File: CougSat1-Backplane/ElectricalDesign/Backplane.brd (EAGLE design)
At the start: 82.8 x 86 mm, 17 parts, among them J1 CougSat Socket, J10 CougSat Socket, J2 CougSat Socket, J3 CougSat Socket, J4 CougSat Socket, J5 Separation Switch, J6 Separation Switch, J7 CougSat Socket, J8 CougSat Socket, J9 CougSat Socket

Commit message: Added balancing and silkscreen decals
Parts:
- added LOGO100: Satellite 16mm, CougsInSpace-Aesthetics:CIS-SATELLITE-16
- added LOGO2: SIGNATUREHENDRIK, CougsInSpace-Aesthetics:SIGN-HENDRIK
- LOGO1: value SIGNATUREHENDRIK -> Text; device CougsInSpace-Aesthetics:SIGN-HENDRIK -> CougsInSpace-Aesthetics:CIS-TEXT
- moved LOGO1 40.6 mm to (-25.3, 0.00)
- moved H1 28.0 mm to (-14.0, 0.00)
- moved H2 28.0 mm to (14.0, 0.00)
- moved C1 19.3 mm to (-9.50, -1.80), turned to 270 degrees
- moved C2 19.0 mm to (9.50, -1.80)
- moved R2 3.60 mm to (9.50, 1.80), turned to 270 degrees
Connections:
- net CHASSIS1: now also C1.1, H1.1, H1.V1, H1.V2, H1.V3, H1.V4, H1.V5, H1.V6, H1.V7, H1.V8; no longer C2.1, H2.1, H2.V1, H2.V2, H2.V3, H2.V4, H2.V5, H2.V6, H2.V7, H2.V8
- net CHASSIS2: now also C2.1, H2.1, H2.V1, H2.V2, H2.V3, H2.V4, H2.V5, H2.V6, H2.V7, H2.V8; no longer C1.1, H1.1, H1.V1, H1.V2, H1.V3, H1.V4, H1.V5, H1.V6, H1.V7, H1.V8
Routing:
- net PGND: track 395.8 -> 389.8 mm
- net CHASSIS2: track 25.9 -> 26.5 mm
- added copper zone on layer 1, net BALANCING-TOP
- added copper zone on layer 16, net BALANCING-TOP
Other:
- board text added: "Backplane V3.0 1915"

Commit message: Final asthetic changes, re-exported pdfs
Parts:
- moved LOGO100 25.8 mm to (-29.2, 25.7), flipped to the top
- moved J5 3.00 mm to (-29.0, 0.00)
- moved J6 3.00 mm to (29.0, 0.00)
- moved LOGO2 0.50 mm to (25.5, 0.00)
- moved LOGO1 0.10 mm to (-25.2, 0.00), flipped to the bottom
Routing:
- net PWR_CTRL_SW: track 218.1 -> 214.4 mm
- net PGND: track 389.8 -> 386.1 mm
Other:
- board text added: "Backplane V3.0"
- board text added: "Slot 0"
- board text added: "Slot 1"
- board text added: "Slot 2"
- board text added: "Slot 3"
- board text added: "Slot 4"
- board text added: "Slot 5"
- board text added: "Slot 6"
- board text added: "Slot 7"
- board text removed: "Backplane V3.0 1915"

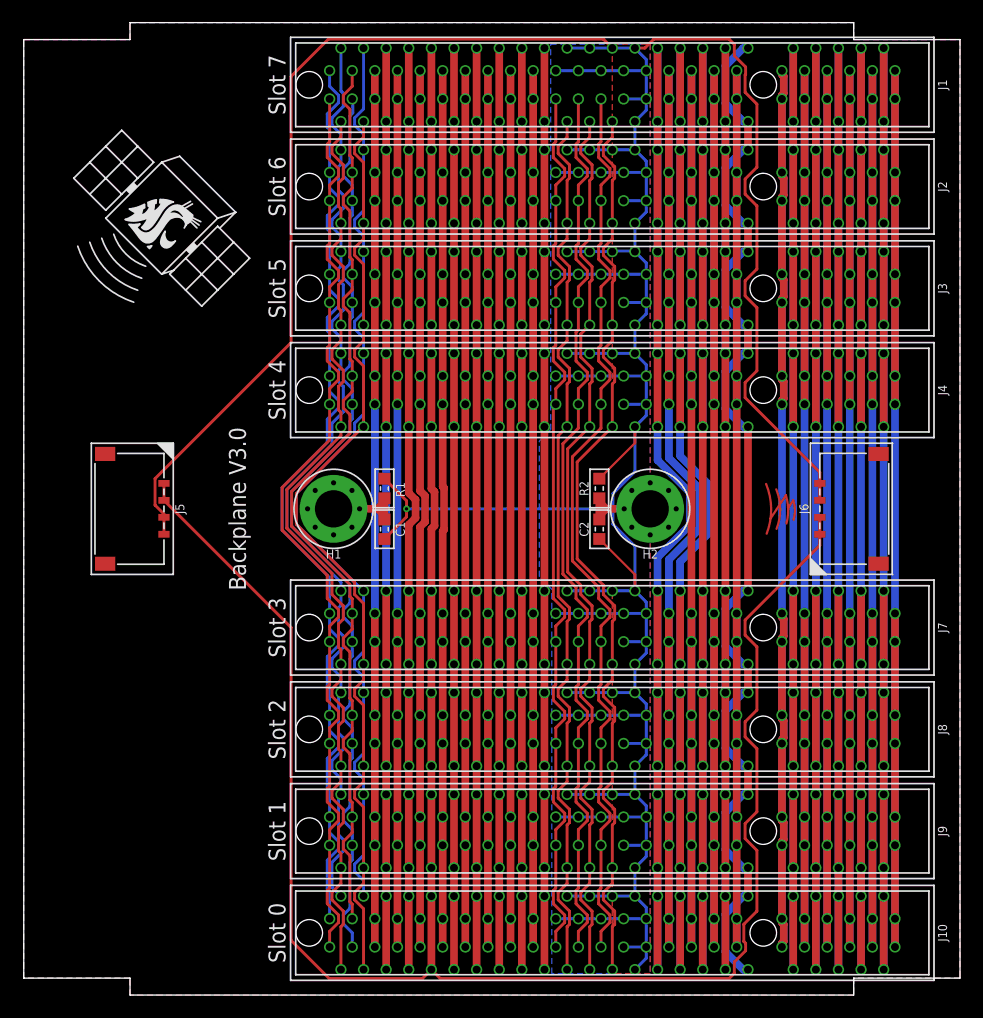
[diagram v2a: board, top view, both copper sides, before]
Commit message: Fixed dimension errors, updated signature
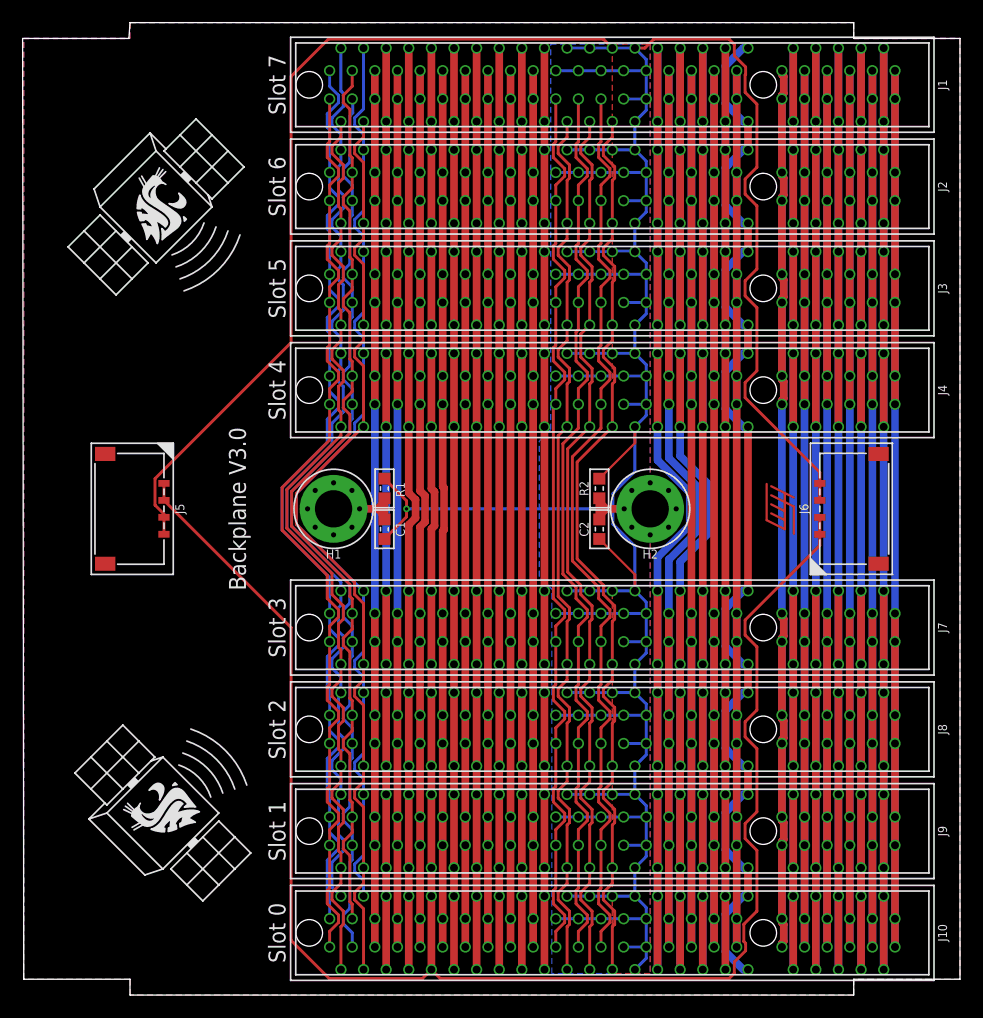
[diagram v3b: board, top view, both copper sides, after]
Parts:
- added LOGO3: Satellite 16mm, CougsInSpace-Aesthetics:CIS-SATELLITE-16
- moved LOGO1 3.20 mm to (-28.4, 0.10)
- moved LOGO100 1.12 mm to (-29.7, 26.7), turned to 90 degrees
- turned LOGO2 to 270 degrees
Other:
- board size 82.8 x 86 mm -> 82.9 x 86 mm
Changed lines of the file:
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@@
 <setting verticaltext="up"/>
 </settings>
-<grid distance="0.25" unitdist="mm" unit="mm" style="lines" multiple="1" display="yes" altdistance="0.05" altunitdist="mm" altunit="mm"/>
+<grid distance="0.1" unitdist="mm" unit="mm" style="lines" multiple="1" display="yes" altdistance="0.005" altunitdist="mm" altunit="mm"/>
 <layers>
 <layer number="1" name="Top" color="4" fill="1" visible="yes" active="yes"/>
@@
 <board>
 <plain>
-<wire x1="41.4" y1="-41.5" x2="32" y2="-41.5" width="0" layer="20"/>
-<wire x1="32" y1="-41.5" x2="32" y2="-43" width="0" layer="20"/>
+<wire x1="41.4" y1="-41.6" x2="32" y2="-41.6" width="0" layer="20"/>
+<wire x1="32" y1="-41.6" x2="32" y2="-43" width="0" layer="20"/>
 <wire x1="32" y1="-43" x2="-32" y2="-43" width="0" layer="20"/>
-<wire x1="-32" y1="-43" x2="-32" y2="-41.5" width="0" layer="20"/>
-<wire x1="-32" y1="-41.5" x2="-41.4" y2="-41.5" width="0" layer="20"/>
-<wire x1="-41.4" y1="-41.5" x2="-41.4" y2="41.5" width="0" layer="20"/>
-<wire x1="-41.4" y1="41.5" x2="-32" y2="41.5" width="0" layer="20"/>
-<wire x1="-32" y1="41.5" x2="-32" y2="43" width="0" layer="20"/>
+<wire x1="-32" y1="-43" x2="-32" y2="-41.6" width="0" layer="20"/>
+<wire x1="-32" y1="-41.6" x2="-41.4" y2="-41.6" width="0" layer="20"/>
+<wire x1="-41.4" y1="-41.6" x2="-41.5" y2="41.6" width="0" layer="20"/>
+<wire x1="-41.5" y1="41.6" x2="-32.1" y2="41.6" width="0" layer="20"/>
+<wire x1="-32.1" y1="41.6" x2="-32" y2="43" width="0" layer="20"/>
 <wire x1="-32" y1="43" x2="32" y2="43" width="0" layer="20"/>
-<wire x1="32" y1="43" x2="32" y2="41.5" width="0" layer="20"/>
-<wire x1="32" y1="41.5" x2="41.4" y2="41.5" width="0" layer="20"/>
-<wire x1="41.4" y1="41.5" x2="41.4" y2="-41.5" width="0" layer="20"/>
+<wire x1="32" y1="43" x2="32" y2="41.6" width="0" layer="20"/>
+<wire x1="32" y1="41.6" x2="41.4" y2="41.6" width="0" layer="20"/>
+<wire x1="41.4" y1="41.6" x2="41.4" y2="-41.6" width="0" layer="20"/>
 <text x="-22.5" y="0" size="1.5" layer="21" font="vector" ratio="15" rot="R90" align="center">Backplane V3.0</text>
 <text x="-19" y="-37.5" size="1.5" layer="21" font="vector" ratio="15" rot="R270" align="center">Slot 0</text>
@@
 <attribute name="TEMP" value="70°C Max 2A" x="-85.75" y="-37.57" size="1.778" layer="27" rot="R270" display="off"/>
 </element>
-<element name="LOGO2" library="CougsInSpace-Aesthetics" package="SIGN-HENDRIK" value="SIGNATUREHENDRIK" x="25.5" y="0" smashed="yes"/>
-<element name="LOGO1" library="CougsInSpace-Aesthetics" package="CIS-TEXT" value="Text" x="-25.2" y="0" smashed="yes" rot="MR90"/>
-<element name="LOGO100" library="CougsInSpace-Aesthetics" package="CIS-SATELLITE-16" value="Satellite 16mm" x="-29.2" y="25.7" smashed="yes"/>
+<element name="LOGO2" library="CougsInSpace-Aesthetics" package="SIGN-HENDRIK" value="SIGNATUREHENDRIK" x="25.5" y="0" smashed="yes" rot="R270"/>
+<element name="LOGO1" library="CougsInSpace-Aesthetics" package="CIS-TEXT" value="Text" x="-28.4" y="0.1" smashed="yes" rot="MR90"/>
+<element name="LOGO100" library="CougsInSpace-Aesthetics" package="CIS-SATELLITE-16" value="Satellite 16mm" x="-29.7" y="26.7" smashed="yes" rot="R90"/>
+<element name="LOGO3" library="CougsInSpace-Aesthetics" package="CIS-SATELLITE-16" value="Satellite 16mm" x="-29.1" y="-26.9" smashed="yes" rot="R180"/>
 </elements>
 <signals>
@@
 <signal name="BALANCING-TOP">
 <polygon width="0.16" layer="1" spacing="0.5" pour="hatch" rank="6">
-<vertex x="-41.4" y="41.5"/>
-<vertex x="-32" y="41.5"/>
+<vertex x="-41.4" y="41.6"/>
+<vertex x="-32" y="41.6"/>
 <vertex x="-32" y="43"/>
 <vertex x="32" y="43"/>
-<vertex x="32" y="41.5"/>
-<vertex x="41.4" y="41.5"/>
-<vertex x="41.4" y="-41.5"/>
-<vertex x="32" y="-41.5"/>
+<vertex x="32" y="41.6"/>
+<vertex x="41.4" y="41.6"/>
+<vertex x="41.4" y="-41.6"/>
+<vertex x="32" y="-41.6"/>
 <vertex x="32" y="-43"/>
 <vertex x="-32" y="-43"/>
-<vertex x="-32" y="-41.5"/>
-<vertex x="-41.4" y="-41.5"/>
+<vertex x="-32" y="-41.6"/>
+<vertex x="-41.4" y="-41.6"/>
 </polygon>
 <polygon width="0.16" layer="16" spacing="0.5" pour="hatch" rank="6">
-<vertex x="-41.4" y="41.5"/>
-<vertex x="-32" y="41.5"/>
+<vertex x="-41.4" y="41.6"/>
+<vertex x="-32" y="41.6"/>
 <vertex x="-32" y="43"/>
 <vertex x="32" y="43"/>
-<vertex x="32" y="41.5"/>
-<vertex x="41.4" y="41.5"/>
-<vertex x="41.4" y="-41.5"/>
-<vertex x="32" y="-41.5"/>
+<vertex x="32" y="41.6"/>
+<vertex x="41.4" y="41.6"/>
+<vertex x="41.4" y="-41.6"/>
+<vertex x="32" y="-41.6"/>
 <vertex x="32" y="-43"/>
 <vertex x="-32" y="-43"/>
-<vertex x="-32" y="-41.5"/>
-<vertex x="-41.4" y="-41.5"/>
+<vertex x="-32" y="-41.6"/>
+<vertex x="-41.4" y="-41.6"/>
 </polygon>
 </signal>
 </signals>
 <mfgpreviewcolors>
-<mfgpreviewcolor name="soldermaskcolor" color="0xC8008000"/>
+<mfgpreviewcolor name="soldermaskcolor" color="0xC8FF0000"/>
 <mfgpreviewcolor name="silkscreencolor" color="0xFFFEFEFE"/>
 <mfgpreviewcolor name="backgroundcolor" color="0xFF282828"/>

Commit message: Fixed Board Outline and Updated mCAD
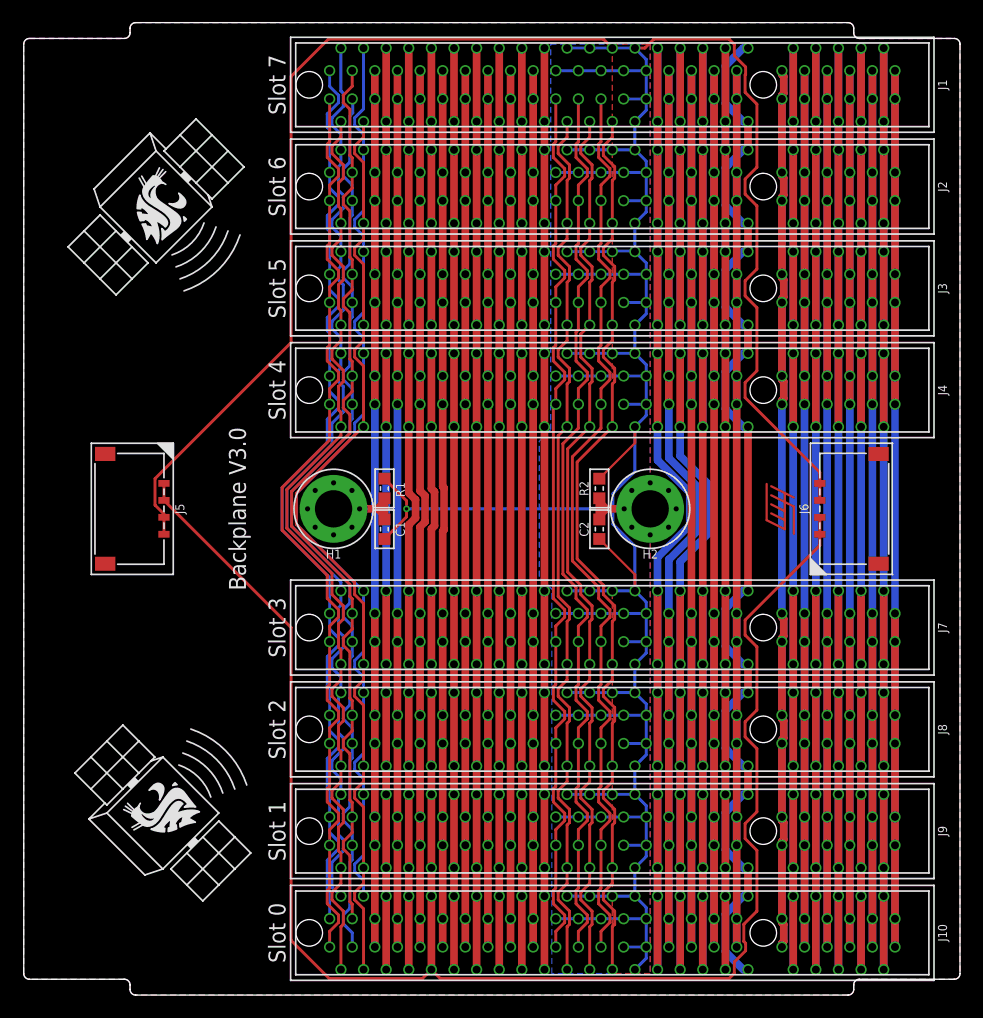
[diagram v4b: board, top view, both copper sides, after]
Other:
- board size 82.9 x 86 mm -> 82.8 x 86 mm
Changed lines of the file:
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@@
 <board>
 <plain>
-<wire x1="41.4" y1="-41.6" x2="32" y2="-41.6" width="0" layer="20"/>
-<wire x1="32" y1="-41.6" x2="32" y2="-43" width="0" layer="20"/>
-<wire x1="32" y1="-43" x2="-32" y2="-43" width="0" layer="20"/>
-<wire x1="-32" y1="-43" x2="-32" y2="-41.6" width="0" layer="20"/>
-<wire x1="-32" y1="-41.6" x2="-41.4" y2="-41.6" width="0" layer="20"/>
-<wire x1="-41.4" y1="-41.6" x2="-41.5" y2="41.6" width="0" layer="20"/>
-<wire x1="-41.5" y1="41.6" x2="-32.1" y2="41.6" width="0" layer="20"/>
-<wire x1="-32.1" y1="41.6" x2="-32" y2="43" width="0" layer="20"/>
-<wire x1="-32" y1="43" x2="32" y2="43" width="0" layer="20"/>
-<wire x1="32" y1="43" x2="32" y2="41.6" width="0" layer="20"/>
-<wire x1="32" y1="41.6" x2="41.4" y2="41.6" width="0" layer="20"/>
-<wire x1="41.4" y1="41.6" x2="41.4" y2="-41.6" width="0" layer="20"/>
+<wire x1="-31.5" y1="43" x2="31.5" y2="43" width="0" layer="20"/>
+<wire x1="31.5" y1="43" x2="32" y2="42.5" width="0" layer="20" curve="-90"/>
+<wire x1="32" y1="42.5" x2="32" y2="42.1" width="0" layer="20"/>
+<wire x1="32" y1="42.1" x2="32.5" y2="41.6" width="0" layer="20" curve="90"/>
+<wire x1="32.5" y1="41.6" x2="40.9" y2="41.6" width="0" layer="20"/>
+<wire x1="40.9" y1="41.6" x2="41.4" y2="41.1" width="0" layer="20" curve="-90"/>
+<wire x1="41.4" y1="41.1" x2="41.4" y2="-41.1" width="0" layer="20"/>
+<wire x1="41.4" y1="-41.1" x2="40.9" y2="-41.6" width="0" layer="20" curve="-90"/>
+<wire x1="40.9" y1="-41.6" x2="32.5" y2="-41.6" width="0" layer="20"/>
+<wire x1="32.5" y1="-41.6" x2="32" y2="-42.1" width="0" layer="20" curve="90"/>
+<wire x1="32" y1="-42.1" x2="32" y2="-42.5" width="0" layer="20"/>
+<wire x1="32" y1="-42.5" x2="31.5" y2="-43" width="0" layer="20" curve="-90"/>
+<wire x1="31.5" y1="-43" x2="-31.5" y2="-43" width="0" layer="20"/>
+<wire x1="-31.5" y1="-43" x2="-32" y2="-42.5" width="0" layer="20" curve="-90"/>
+<wire x1="-32" y1="-42.5" x2="-32" y2="-42.1" width="0" layer="20"/>
+<wire x1="-32" y1="-42.1" x2="-32.5" y2="-41.6" width="0" layer="20" curve="90"/>
+<wire x1="-32.5" y1="-41.6" x2="-40.9" y2="-41.6" width="0" layer="20"/>
+<wire x1="-40.9" y1="-41.6" x2="-41.4" y2="-41.1" width="0" layer="20" curve="-90"/>
+<wire x1="-41.4" y1="-41.1" x2="-41.4" y2="41.1" width="0" layer="20"/>
+<wire x1="-41.4" y1="41.1" x2="-40.9" y2="41.6" width="0" layer="20" curve="-90"/>
+<wire x1="-40.9" y1="41.6" x2="-32.5" y2="41.6" width="0" layer="20"/>
+<wire x1="-32.5" y1="41.6" x2="-32" y2="42.1" width="0" layer="20" curve="90"/>
+<wire x1="-32" y1="42.1" x2="-32" y2="42.5" width="0" layer="20"/>
+<wire x1="-32" y1="42.5" x2="-31.5" y2="43" width="0" layer="20" curve="-90"/>
 <text x="-22.5" y="0" size="1.5" layer="21" font="vector" ratio="15" rot="R90" align="center">Backplane V3.0</text>
 <text x="-19" y="-37.5" size="1.5" layer="21" font="vector" ratio="15" rot="R270" align="center">Slot 0</text>
@@
 <signal name="BALANCING-TOP">
 <polygon width="0.16" layer="1" spacing="0.5" pour="hatch" rank="6">
-<vertex x="-41.4" y="41.6"/>
-<vertex x="-32" y="41.6"/>
-<vertex x="-32" y="43"/>
-<vertex x="32" y="43"/>
-<vertex x="32" y="41.6"/>
-<vertex x="41.4" y="41.6"/>
-<vertex x="41.4" y="-41.6"/>
-<vertex x="32" y="-41.6"/>
-<vertex x="32" y="-43"/>
-<vertex x="-32" y="-43"/>
-<vertex x="-32" y="-41.6"/>
-<vertex x="-41.4" y="-41.6"/>
+<vertex x="-31.5" y="43"/>
+<vertex x="31.5" y="43" curve="-90"/>
+<vertex x="32" y="42.5"/>
+<vertex x="32" y="42.1" curve="90"/>
+<vertex x="32.5" y="41.6"/>
+<vertex x="40.9" y="41.6" curve="-90"/>
+<vertex x="41.4" y="41.1"/>
+<vertex x="41.4" y="-41.1" curve="-90"/>
+<vertex x="40.9" y="-41.6"/>
+<vertex x="32.5" y="-41.6" curve="90"/>
+<vertex x="32" y="-42.1"/>
+<vertex x="32" y="-42.5" curve="-90"/>
+<vertex x="31.5" y="-43"/>
+<vertex x="-31.5" y="-43" curve="-90"/>
+<vertex x="-32" y="-42.5"/>
+<vertex x="-32" y="-42.1" curve="90"/>
+<vertex x="-32.5" y="-41.6"/>
+<vertex x="-40.9" y="-41.6" curve="-90"/>
+<vertex x="-41.4" y="-41.1"/>
+<vertex x="-41.4" y="41.1" curve="-90"/>
+<vertex x="-40.9" y="41.6"/>
+<vertex x="-32.5" y="41.6" curve="90"/>
+<vertex x="-32" y="42.1"/>
+<vertex x="-32" y="42.5" curve="-90"/>
 </polygon>
 <polygon width="0.16" layer="16" spacing="0.5" pour="hatch" rank="6">
-<vertex x="-41.4" y="41.6"/>
-<vertex x="-32" y="41.6"/>
-<vertex x="-32" y="43"/>
-<vertex x="32" y="43"/>
-<vertex x="32" y="41.6"/>
-<vertex x="41.4" y="41.6"/>
-<vertex x="41.4" y="-41.6"/>
-<vertex x="32" y="-41.6"/>
-<vertex x="32" y="-43"/>
-<vertex x="-32" y="-43"/>
-<vertex x="-32" y="-41.6"/>
-<vertex x="-41.4" y="-41.6"/>
+<vertex x="-31.5" y="43"/>
+<vertex x="31.5" y="43" curve="-90"/>
+<vertex x="32" y="42.5"/>
+<vertex x="32" y="42.1" curve="90"/>
+<vertex x="32.5" y="41.6"/>
+<vertex x="40.9" y="41.6" curve="-90"/>
+<vertex x="41.4" y="41.1"/>
+<vertex x="41.4" y="-41.1" curve="-90"/>
+<vertex x="40.9" y="-41.6"/>
+<vertex x="32.5" y="-41.6" curve="90"/>
+<vertex x="32" y="-42.1"/>
+<vertex x="32" y="-42.5" curve="-90"/>
+<vertex x="31.5" y="-43"/>
+<vertex x="-31.5" y="-43" curve="-90"/>
+<vertex x="-32" y="-42.5"/>
+<vertex x="-32" y="-42.1" curve="90"/>
+<vertex x="-32.5" y="-41.6"/>
+<vertex x="-40.9" y="-41.6" curve="-90"/>
+<vertex x="-41.4" y="-41.1"/>
+<vertex x="-41.4" y="41.1" curve="-90"/>
+<vertex x="-40.9" y="41.6"/>
+<vertex x="-32.5" y="41.6" curve="90"/>
+<vertex x="-32" y="42.1"/>
+<vertex x="-32" y="42.5" curve="-90"/>
 </polygon>
 </signal>

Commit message: Fixed errors in board layout
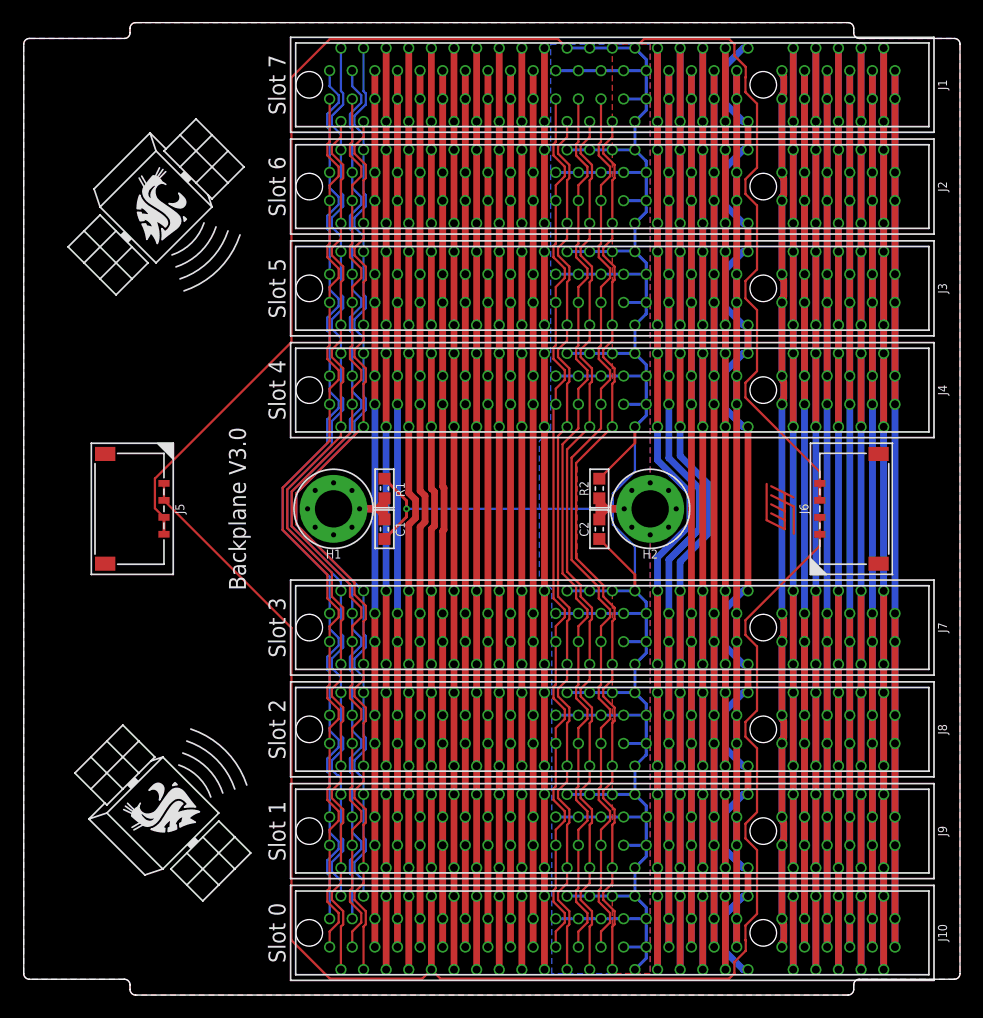
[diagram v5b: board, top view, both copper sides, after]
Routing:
- net PGND: track 386.1 -> 382.0 mm
- net BUS_JTAG_TCK: track 83.9 -> 85.1 mm
- net BUS_JTAG_EN-0: track 83.9 -> 85.1 mm
- net BUS_JTAG_EN-1: track 83.8 -> 85.1 mm
- net BUS_JTAG_TDI: track 83.9 -> 85.1 mm
- net BUS_JTAG_TDO: track 85.1 -> 84.1 mm
- net BUS_JTAG_EN-2: track 85.1 -> 84.1 mm
